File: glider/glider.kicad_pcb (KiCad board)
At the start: 4 copper layers, 40 x 80 mm, 127 parts, among them J1 SENSOR_I2C, J10 CELL, J11 SCH1, J12 IO, J13 SCH2, J14 SCH3, J15 SCH4, J16 SCH5, J17 SCH6, J18 SCH7, J19 Micro_SD_Card, J2 USB_B_Micro, J20 Conn_01x02, J3 NCP_EXT, J4 DEBUG_NAV, J5 DEBUG_NCP, J6 SCH8, J7 GPS_UART, J8 NCP_COM, J9 IMU_SPI, Q1 Q_PMOS_DGS, SW1 NAV_NRST, SW2 NAV_BOOT, SW3 NCP_NRST, SW4 NCP_USER, U1 BGM220P, U10 AP2120N-1.8, U11 FXLA0104, U12 RT6218A, U2 STM32G484RETx, U3 MCP1812, U4 MCP73831-2-OT, U5 MS5637, U6 W25N01GVZEIG, U7 ICM-20948, U8 L96-M33, U9 AP22804, Y1 8MHz

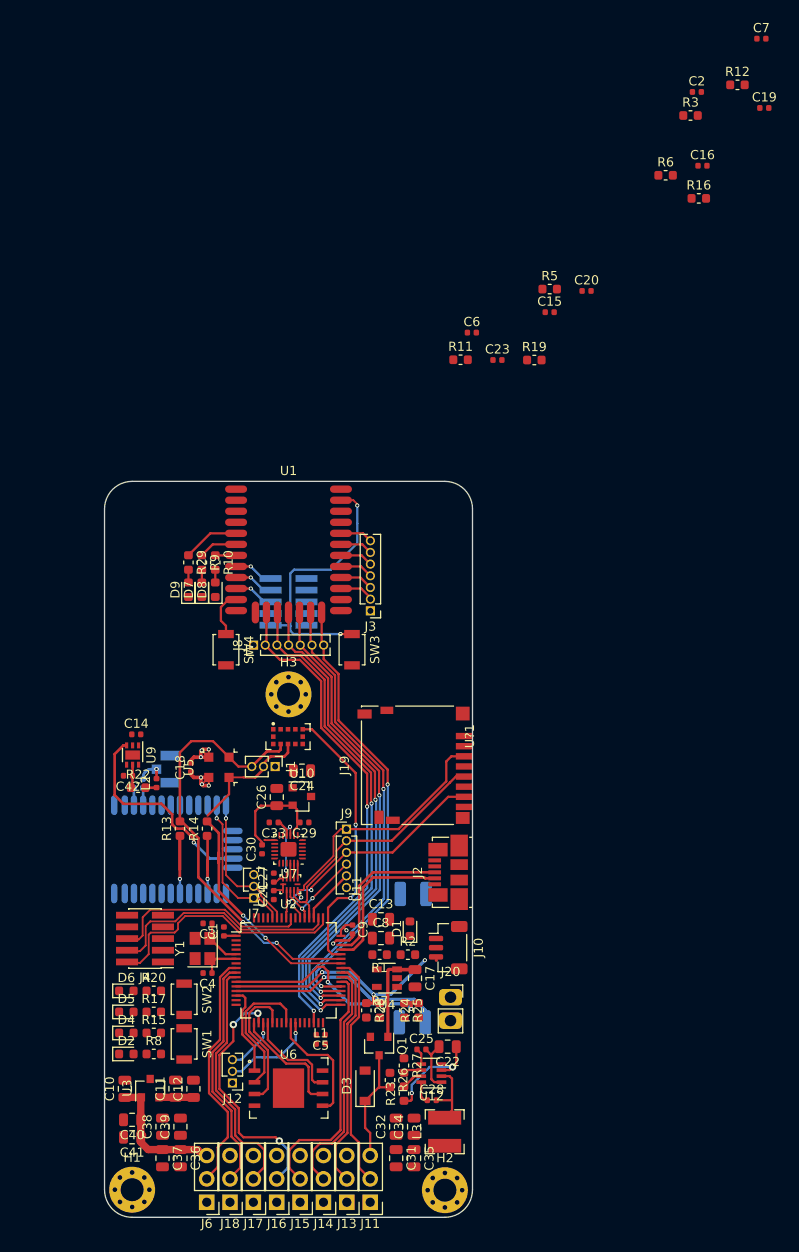
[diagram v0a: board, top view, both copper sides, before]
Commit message: all components placed, initial board art
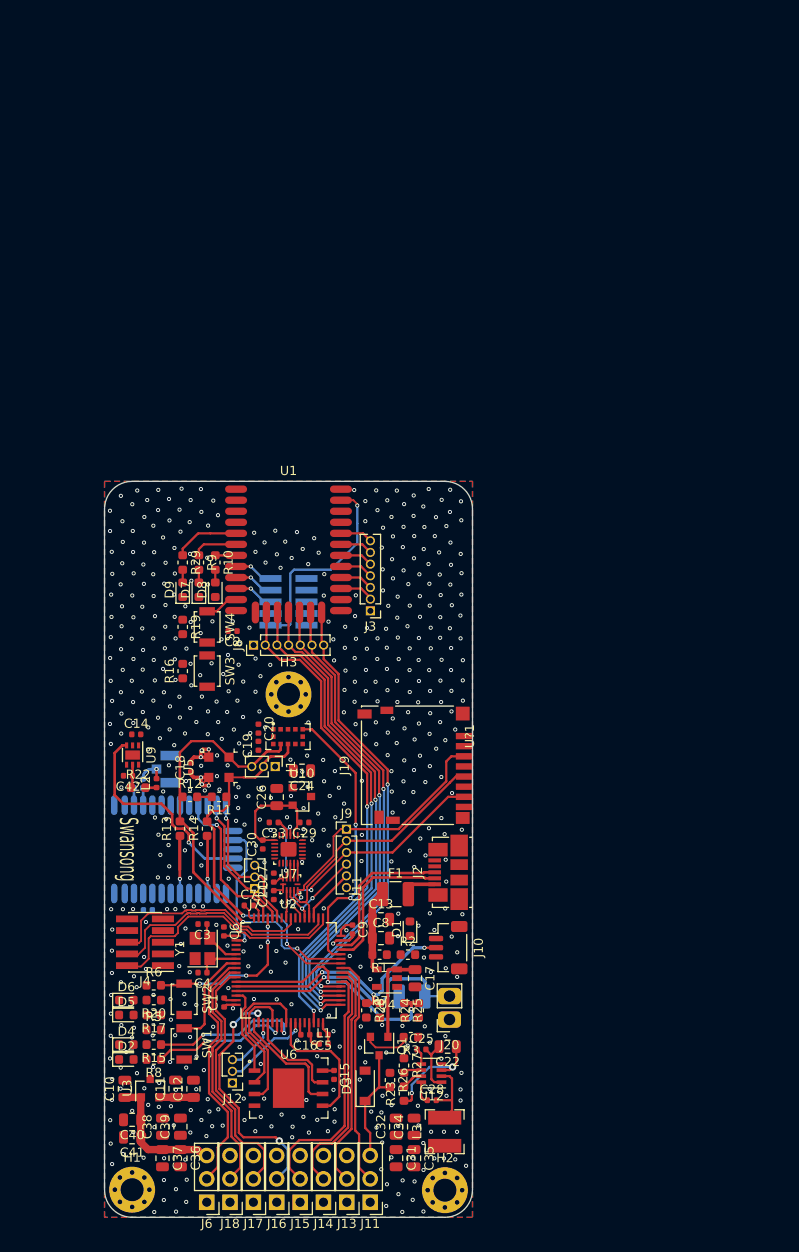
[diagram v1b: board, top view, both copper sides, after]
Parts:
- added G***: LOGO, atlas:boardartneg, B.Cu at (58.8, 130.4)
- C23: moved to B.Cu
- F1: moved to F.Cu
- moved C7 109.5 mm to (55.7, 136.1)
- moved R3 104.7 mm to (73.3, 150.4), turned to 180 degrees
- moved R6 104.2 mm to (45.4, 144.8)
- moved C16 103.9 mm to (61.8, 150.2), turned to 180 degrees
- moved R12 97.6 mm to (49.3, 124.3)
- moved R5 91.3 mm to (45.4, 149.6)
- moved C19 88.5 mm to (56.7, 118.7), turned to 90 degrees
- moved C15 86.2 mm to (65.0, 154.5), turned to 270 degrees
- moved C2 77.3 mm to (53.9, 106.3), turned to 180 degrees
- moved R16 76.1 mm to (48.5, 110.6), turned to 90 degrees
- moved C23 70.8 mm to (44.7, 136.6), turned to 180 degrees
- moved C6 70.5 mm to (53.0, 138.9), turned to 270 degrees
- moved C20 59.5 mm to (56.7, 116.9), turned to 270 degrees
- moved R11 54.3 mm to (52.5, 124.3), turned to 180 degrees
- moved R19 48.0 mm to (48.5, 105.8), turned to 270 degrees
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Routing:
- net /NAV_BOOT: track 0.00 -> 17.6 mm, vias 0 -> 4
- net /GPS_RESET: track 0.00 -> 16.9 mm, vias 0 -> 1
- net /NAV_STAT_1: track 0.00 -> 16.8 mm, vias 0 -> 2
- net /NAV_STAT_0: track 0.00 -> 15.5 mm, vias 0 -> 2
- net Net-(C13-Pad1): track 0.00 -> 14.2 mm
- net /GPS_FORCEON: track 0.00 -> 13.9 mm, vias 0 -> 1
- net /NAV_NRST: track 0.00 -> 11.0 mm
- net /VDD_MCU: track 15.8 -> 24.9 mm
- net /NCP_NRST: track 30.6 -> 22.6 mm, vias 2 -> 1
- net /OPAMP3_CELL_IS: track 24.0 -> 28.7 mm
- net GND: track 15.5 -> 19.7 mm, vias 4 -> 560
- net Net-(F1-Pad2): track 0.00 -> 3.68 mm
- net Net-(C16-Pad1): track 0.00 -> 3.13 mm
- net /ADC1_IN1_CELL_TS: track 26.1 -> 28.7 mm
- net /SENSOR_I2C_SDA: track 39.8 -> 41.9 mm
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- added copper zone on B.Cu, net GND
- added copper zone on F.Cu, net GND
- added copper zone on In1.Cu, net GND
- removed copper zone on In1.Cu, net /VDD_MCU
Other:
- board text added: "Swansong"

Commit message: final checkouts
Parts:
- removed G***: LOGO, atlas:boardartneg
- removed J10: CELL, Connector_JST:JST_SH_BM03B-SRSS-TB_1x03-1MP_P1.00mm_Vertical
- added C43: 4.7u, Capacitor_SMD:C_0805_2012Metric, F.Cu at (49.8, 157.2)
- added C44: 4.7u, Capacitor_SMD:C_0805_2012Metric, F.Cu at (42.6, 156.5)
- added LS1: PKLCS1212E40A1-R1, atlas:PKLCS1212, B.Cu at (73.3, 155.9)
- added Q2: 2N7002E, Package_TO_SOT_SMD:SOT-23, F.Cu at (56.1, 126.9)
- added Q3: 2N7002E, Package_TO_SOT_SMD:SOT-23, B.Cu at (65.3, 152.1)
- added R30: 100k, Resistor_SMD:R_0603_1608Metric, F.Cu at (56.0, 124.3)
- added R31: 1k, Resistor_SMD:R_0603_1608Metric, B.Cu at (66.3, 155.9)
- C15: value C_Small -> 0.1u
- C22, C31, C32, C34, C35, C36, C37, C38, C39, C40, C41: value 22u -> 10u
- D7: value NAV_STAT_1 -> NCP_STAT1
- D9: value NAV_STAT_0 -> NCP_STAT0
- J20: value Conn_01x02 -> CELL; footprint Connector_PinSocket_2.54mm:PinSocket_1x02_P2.54mm_Vertical -> Connector_PinSocket_2.54mm:PinSocket_1x03_P2.54mm_Vertical
- J3: footprint Connector_PinHeader_1.27mm:PinHeader_1x07_P1.27mm_Vertical -> Connector_PinHeader_1.27mm:PinHeader_1x08_P1.27mm_Vertical
- J8: footprint Connector_PinHeader_1.27mm:PinHeader_1x07_P1.27mm_Vertical -> Connector_PinHeader_2.54mm:PinHeader_1x08_P2.54mm_Vertical
- Q1: value Q_PMOS_DGS -> DMP1045UQ
- R1: value 2k -> 10k
- R13, R14: footprint Resistor_SMD:R_0603_1608Metric -> Resistor_SMD:R_0402_1005Metric
- R25: value 10k -> 100k
- R28, R7: moved to B.Cu
- SW1, SW2, SW3, SW4: footprint Button_Switch_SMD:SW_SPST_B3U-1000P -> Button_Switch_SMD:SW_SPST_PTS810
- U10: value AP2120N-1.8 -> MIC5501-3.0YM5; footprint Package_TO_SOT_SMD:SOT-23 -> Package_TO_SOT_SMD:SOT-23-5
- U11: value FXLA0104 -> NTB0104; footprint atlas:UMLP-12 -> atlas:WQFN-14-1EP_2.5x3mm_P0.5mm_EP1.45x1.00mm
- U3: value MCP1812 -> MIC5504-1.8YM5; footprint Package_TO_SOT_SMD:SOT-23 -> Package_TO_SOT_SMD:SOT-23-5
- moved U3 35.8 mm to (61.8, 124.4), turned to 180 degrees
- moved U10 35.6 mm to (46.2, 156.5)
- moved R19 14.0 mm to (42.7, 118.5), turned to 0 degrees
- moved SW4 13.0 mm to (43.0, 115.9), turned to 180 degrees
- moved C14 11.3 mm to (46.1, 128.5), turned to 180 degrees
- moved R16 11.1 mm to (42.7, 120.1), turned to 0 degrees
- moved J20 9.46 mm to (77.9, 139.1), turned to 0 degrees
- moved R7 8.42 mm to (74.7, 140.6), turned to 270 degrees
- moved R28 8.41 mm to (73.2, 140.6), turned to 90 degrees
- moved U9 7.25 mm to (46.5, 126.1), turned to 90 degrees
- moved R6 5.80 mm to (48.4, 149.7), turned to 270 degrees
- moved SW3 5.79 mm to (48.7, 115.9), turned to 180 degrees
- moved SW2 5.68 mm to (43.0, 146.2), turned to 180 degrees
- moved R1 5.34 mm to (70.9, 146.7)
- moved SW1 5.00 mm to (48.7, 146.2), turned to 0 degrees
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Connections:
- C24 pad 1: /VDD_SYS -> /VDD_MCU
- J2 pad 5: Net-(J2-Pad5) -> GND
- J2 pad 6: Net-(J2-Pad5) -> GND
- J20 pad 2: /OPAMP3_CELL_IS -> /ADC1_IN1_CELL_TS
- J3 pad 1: GND -> /VDD_MCU
- J3 pad 2: Net-(J3-Pad2) -> GND
- J4 pad 7: /NCP_SWDIO -> Net-(J4-Pad7)
- J8 pad 1: GND -> /VDD_MCU
- J8 pad 2: /NCP_COM0 -> GND
- J8 pad 3: /NCP_COM1 -> /NCP_COM0
- J8 pad 4: /NCP_COM2 -> /NCP_COM1
- J8 pad 5: /NCP_COM3 -> /NCP_COM2
- J8 pad 6: /NCP_COM4 -> /NCP_COM3
- J8 pad 7: /NCP_COM5 -> /NCP_COM4
- Q1 pad 1: /CELL_POS -> Net-(C13-Pad1)
- Q1 pad 2: Net-(C13-Pad1) -> /VDD_SYS
- Q1 pad 3: /VDD_SYS -> /CELL_POS
- R6 pad 1: /VDD_MCU -> /NAV_BOOT
- R6 pad 2: /NAV_BOOT -> GND
- SW2 pad 1: /NAV_BOOT -> /VDD_MCU
- SW2 pad 2: GND -> /NAV_BOOT
- U1 pad 22: Net-(J3-Pad2) -> Net-(J3-Pad3)
- U1 pad 23: Net-(J3-Pad3) -> Net-(J3-Pad4)
- U1 pad 24: Net-(J3-Pad4) -> Net-(J3-Pad5)
- U1 pad 25: Net-(J3-Pad5) -> Net-(J3-Pad6)
- U1 pad 26: Net-(J3-Pad6) -> Net-(J3-Pad7)
- U1 pad 27: Net-(J3-Pad7) -> Net-(J3-Pad8)
- U10 pad 1: GND -> /VDD_SYS
- U10 pad 2: /VDD_IMU -> GND
- U11 pad 10: /IMU_MISO_LV -> /IMU_MOSI_LV
- U11 pad 11: /VDD_IMU -> /IMU_SCK_LV
- U11 pad 12: /VDD_MCU -> /IMU_NCS_LV
- U11 pad 6: GND -> Net-(U11-Pad6)
- U11 pad 7: /IMU_MOSI_LV -> GND
- U11 pad 8: /IMU_SCK_LV -> /VDD_MCU
- U11 pad 9: /IMU_NCS_LV -> Net-(U11-Pad9)
- U2 pad 44: /TOF_EN -> /BUZZER_TIM2_CH4
- U2 pad 55: Net-(U2-Pad55) -> /TOF_EN
- U3 pad 1: /VDD_SYS -> /VDD_MCU
- U3 pad 2: /VDD_MCU -> GND
- U3 pad 3: GND -> /VDD_MCU
- U6 pad 9: (no net) -> GND
- U7 pad 12: /IMU_INT -> Net-(Q2-Pad1)
- U8 pad 29: /GPS_PPS_LED -> /GPS_PPS
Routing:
- net /VDD_SYS: track 63.3 -> 134.4 mm, vias 0 -> 1
- net /VDD_MCU: track 24.9 -> 85.0 mm, vias 4 -> 36
- net GND: track 19.7 -> 56.4 mm, vias 560 -> 642
- net /GPS_PPS: track 0.00 -> 34.6 mm, vias 0 -> 3
- net /NCP_USER: track 3.68 -> 29.2 mm
- net /NCP_NRST: track 22.6 -> 48.0 mm, vias 1 -> 2
- net /SD_NCS: track 6.04 -> 29.2 mm, vias 0 -> 2
- net /CELL_POS: track 25.8 -> 46.8 mm
- net /GPS_FIX: track 0.00 -> 20.3 mm, vias 0 -> 2
- net Net-(C13-Pad1): track 14.2 -> 32.7 mm
- net /IMU_INT: track 0.00 -> 15.5 mm, vias 0 -> 2
- net Net-(LS1-Pad2): track 0.00 -> 14.9 mm
- net /GPS_EXTINT: track 0.00 -> 13.8 mm, vias 0 -> 1
- net /BUZZER_TIM2_CH4: track 0.00 -> 12.4 mm, vias 0 -> 1
- net Net-(U8-Pad30): track 23.1 -> 11.4 mm
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- added copper zone on In1.Cu, net /VDD_MCU
- removed copper zone on In1.Cu, net GND
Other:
- board text removed: "Swansong"

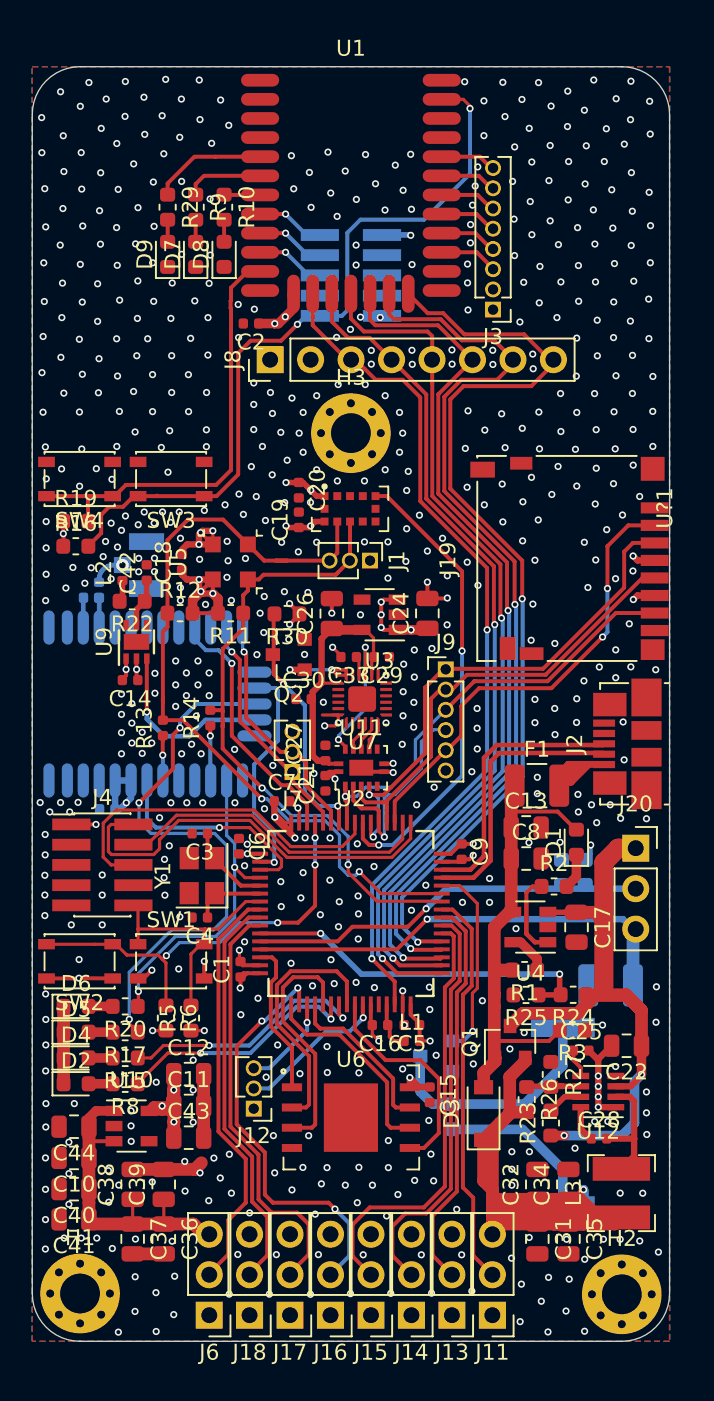
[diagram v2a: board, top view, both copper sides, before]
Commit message: removed bt module again, shrunk board
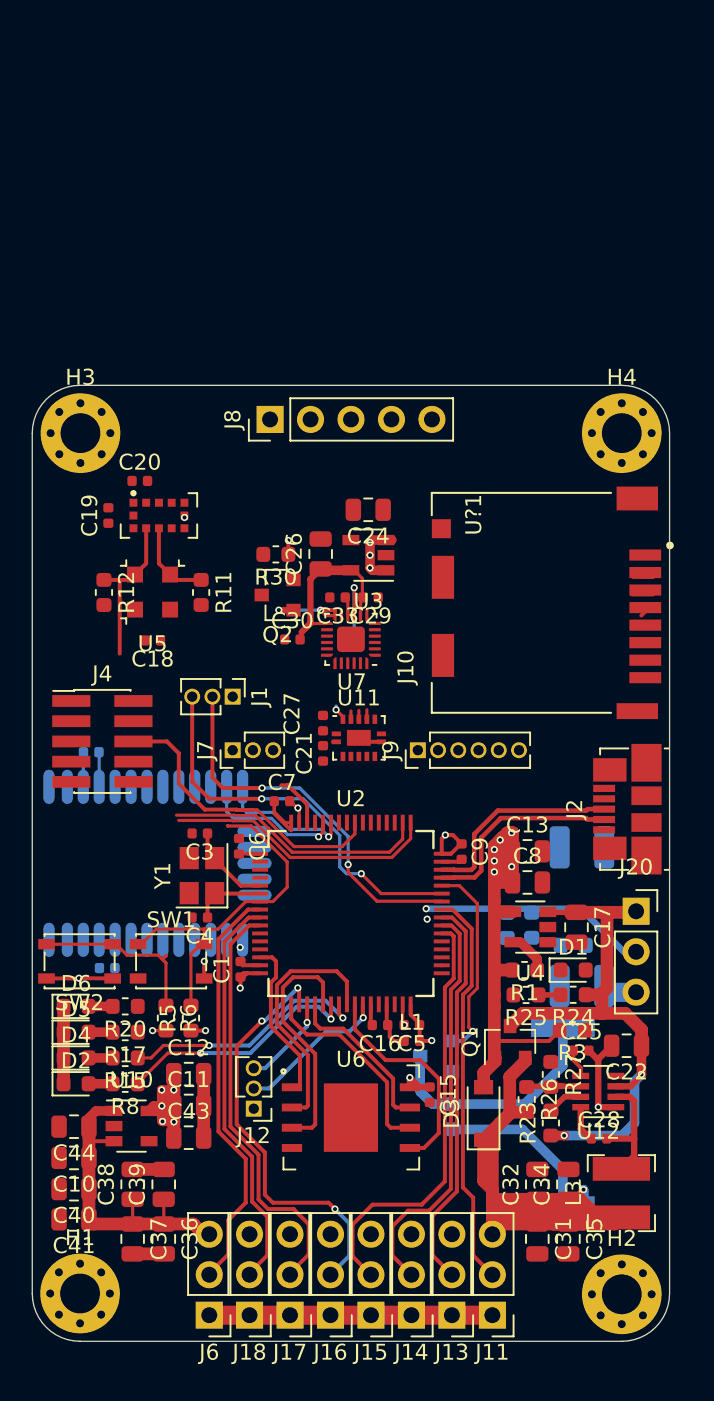
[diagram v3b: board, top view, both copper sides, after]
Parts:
- removed AE1: Antenna_Shield, Connector_Coaxial:U.FL_Hirose_U.FL-R-SMT-1_Vertical
- removed C14, C2, C42: 0.1u, Capacitor_SMD:C_0402_1005Metric
- removed D7: NCP_STAT1, LED_SMD:LED_0603_1608Metric
- removed D8: NAV_STAT_2, LED_SMD:LED_0603_1608Metric
- removed D9: NCP_STAT0, LED_SMD:LED_0603_1608Metric
- removed J19: Micro_SD_Card, Connector_Card:microSD_HC_Hirose_DM3D-SF
- removed J3: NCP_EXT, Connector_PinHeader_1.27mm:PinHeader_1x08_P1.27mm_Vertical
- removed J5: DEBUG_NCP, Connector_PinHeader_1.27mm:PinHeader_2x05_P1.27mm_Vertical_SMD
- removed L2: 47n, Inductor_SMD:L_0402_1005Metric
- removed R10, R29, R9: 1k, Resistor_SMD:R_0603_1608Metric
- removed R13, R14, R21: 0, Resistor_SMD:R_0402_1005Metric
- removed R16, R19: 100k, Resistor_SMD:R_0603_1608Metric
- removed R22: 10, Resistor_SMD:R_0603_1608Metric
- removed SW3: NCP_NRST, Button_Switch_SMD:SW_SPST_PTS810
- removed SW4: NCP_USER, Button_Switch_SMD:SW_SPST_PTS810
- removed U1: BGM220P, atlas:BGM220P
- removed U9: AP22804, Package_DFN_QFN:DFN-6-1EP_2x2mm_P0.65mm_EP1x1.6mm
- added H4: MountingHole_Pad, MountingHole:MountingHole_2.5mm_Pad_Via, F.Cu at (77.0, 113.0)
- added J10: DM3CS-SF, atlas:HRS_DM3CS-SF, F.Cu at (72.1, 123.8)
- F1, R2: moved to B.Cu
- J8: footprint Connector_PinHeader_2.54mm:PinHeader_1x08_P2.54mm_Vertical -> Connector_PinHeader_2.54mm:PinHeader_1x05_P2.54mm_Vertical
- moved H3 17.0 mm to (43.0, 113.0)
- moved J1 12.1 mm to (52.6, 129.5)
- moved U?1 12.0 mm to (48.0, 118.2)
- moved C19 12.0 mm to (44.8, 118.2)
- moved U8 10.00 mm to (40.0, 135.2)
- moved C20 10.00 mm to (46.8, 116.0), turned to 0 degrees
- moved C23 9.98 mm to (44.7, 146.6)
- moved R18 9.70 mm to (43.7, 133.0)
- moved D1 8.03 mm to (74.0, 146.7), turned to 0 degrees
- moved J4 7.75 mm to (44.4, 132.3)
- moved C24 7.49 mm to (61.1, 117.8), turned to 180 degrees
- moved R7 5.92 mm to (69.8, 143.9), turned to 90 degrees
- moved J9 5.37 mm to (64.2, 132.9), turned to 90 degrees
- moved C18 5.25 mm to (47.6, 126.0), turned to 180 degrees
- moved U5 5.24 mm to (47.6, 123.0), turned to 180 degrees
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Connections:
- net /NCP_COM0 renamed /RADIO_USART3_TX
- net /NCP_COM1 renamed /RADIO_USART3_RX
- net /NCP_COM2 renamed /RADIO_SET
- D1 pad 2: Net-(C13-Pad1) -> Net-(D1-Pad2)
- R2 pad 1: Net-(R2-Pad1) -> Net-(D1-Pad2)
- R2 pad 2: Net-(D1-Pad1) -> Net-(C13-Pad1)
- U2 pad 35: /NCP_COM3 -> Net-(U2-Pad35)
- U2 pad 36: /NCP_COM4 -> Net-(U2-Pad36)
- U2 pad 37: /NCP_COM5 -> Net-(U2-Pad37)
- U2 pad 55: /TOF_EN -> Net-(U2-Pad55)
- U4 pad 1: Net-(R2-Pad1) -> Net-(D1-Pad1)
- U8 pad 3: /GPS_I2C_SDA -> Net-(U8-Pad3)
- U8 pad 6: /GPS_I2C_SCL -> Net-(U8-Pad6)
- U?1 pad 5: /TOF_EN -> /VDD_MCU
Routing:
- net /NCP_COM5: track 59.7 -> 0.00 mm, vias 2 -> 0
- net /NCP_COM4: track 57.8 -> 0.00 mm, vias 2 -> 0
- net /NCP_COM3: track 55.5 -> 0.00 mm, vias 2 -> 0
- net /RADIO_SET: track 54.6 -> 0.01 mm, vias 2 -> 0
- net /RADIO_USART3_TX: track 54.0 -> 0.00 mm, vias 2 -> 0
- net /RADIO_USART3_RX: track 54.0 -> 0.00 mm, vias 2 -> 0
- net /NCP_NRST: track 48.0 -> 0.00 mm, vias 2 -> 0
- net /VDD_MCU: track 85.0 -> 46.4 mm, vias 36 -> 15
- net /GPS_PPS: track 34.6 -> 0.00 mm, vias 3 -> 0
- net /IMU_SPI2_MOSI: track 33.8 -> 1.32 mm, vias 2 -> 0
- net /IMU_SPI2_SCK: track 29.4 -> 0.00 mm
- net /TOF_EN: track 29.4 -> 0.00 mm, vias 2 -> 0
- net /NCP_USER: track 29.2 -> 0.00 mm
- net /SD_NCS: track 29.2 -> 1.27 mm, vias 2 -> 0
- net /IMU_SPI2_MISO: track 27.4 -> 0.00 mm, vias 1 -> 0
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- removed copper zone on In1.Cu, net /VDD_MCU
- removed copper zone on B.Cu, net GND
- removed copper zone on F.Cu, net GND
- removed copper zone on In2.Cu, net GND
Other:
- board size 40 x 80 mm -> 40 x 60 mm
